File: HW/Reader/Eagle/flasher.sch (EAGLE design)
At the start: 26 parts, among them Q1 12Mhz, Q1A MMBT3904, Q1B MMBT3904, X1 MINI-USB-SCHIELD-32005-201

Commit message: Flasher CH340G SCH & PCB
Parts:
- removed D1: SS14, diode:DIODE-DO-214AC
- removed R8, R9: 470, rcl:R-US_M0805
- removed RX: (no value), led:LEDCHIP-LED0805
- added P3: (no value), pinhead:PINHD-1X6
- added R2: 470, rcl:R-US_M0805
- renumbered Q1A to T1, Q1B to T2, U$1 to U1
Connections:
- removed net N$7: R9.2, TX.A
- removed net VIN: D1.A, P1.1, P2.1, X1G$1.1
- net +5V: now also P1.1, P2.1, P3.1, X1G$1.1; no longer D1.C, R8.1, R9.1
- net GND: now also P3.6, TX.C
- net GPIO0: now also P3.4
- net N$1: now also R2.2; no longer TX.C
- net N$2: no longer RX.C
- net N$4: now also R2.1, TX.A; no longer R8.2, RX.A
- net RESET: now also P3.5
- net RXD: now also P3.2
- net TXD: now also P3.3
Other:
- note added: "ESP8266 Auto Flasher over USB (CH340G)"
- moved on the sheet: R1, R4, TX

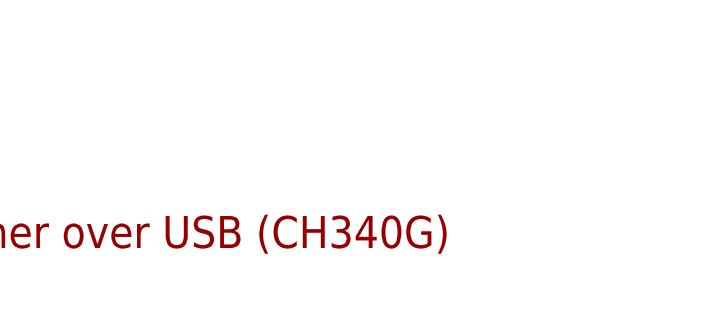
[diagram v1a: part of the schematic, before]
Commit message: Flasher Update
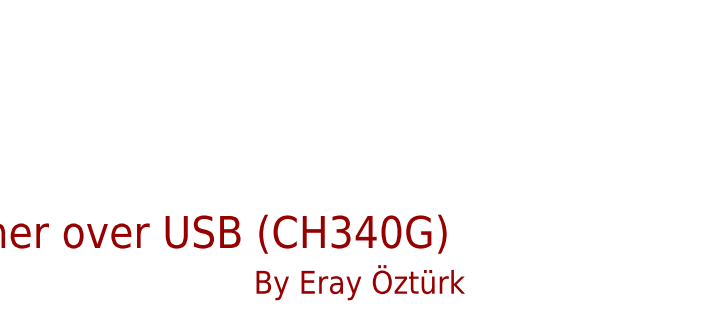
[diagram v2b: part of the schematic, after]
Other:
- note added: "By Eray Öztürk"
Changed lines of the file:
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@@
 <grid distance="0.1" unitdist="inch" unit="inch" style="lines" multiple="1" display="no" altdistance="0.01" altunitdist="inch" altunit="inch"/>
 <layers>
-<layer number="1" name="Top" color="4" fill="1" visible="no" active="no"/>
-<layer number="16" name="Bottom" color="1" fill="1" visible="no" active="no"/>
-<layer number="17" name="Pads" color="2" fill="1" visible="no" active="no"/>
-<layer number="18" name="Vias" color="2" fill="1" visible="no" active="no"/>
-<layer number="19" name="Unrouted" color="6" fill="1" visible="no" active="no"/>
-<layer number="20" name="Dimension" color="24" fill="1" visible="no" active="no"/>
-<layer number="21" name="tPlace" color="7" fill="1" visible="no" active="no"/>
-<layer number="22" name="bPlace" color="7" fill="1" visible="no" active="no"/>
-<layer number="23" name="tOrigins" color="15" fill="1" visible="no" active="no"/>
-<layer number="24" name="bOrigins" color="15" fill="1" visible="no" active="no"/>
-<layer number="25" name="tNames" color="7" fill="1" visible="no" active="no"/>
-<layer number="26" name="bNames" color="7" fill="1" visible="no" active="no"/>
-<layer number="27" name="tValues" color="7" fill="1" visible="no" active="no"/>
-<layer number="28" name="bValues" color="7" fill="1" visible="no" active="no"/>
+<layer number="1" name="Top" color="4" fill="1" visible="yes" active="no"/>
+<layer number="16" name="Bottom" color="1" fill="1" visible="yes" active="no"/>
+<layer number="17" name="Pads" color="2" fill="1" visible="yes" active="no"/>
+<layer number="18" name="Vias" color="2" fill="1" visible="yes" active="no"/>
+<layer number="19" name="Unrouted" color="6" fill="1" visible="yes" active="no"/>
+<layer number="20" name="Dimension" color="24" fill="1" visible="yes" active="no"/>
+<layer number="21" name="tPlace" color="7" fill="1" visible="yes" active="no"/>
+<layer number="22" name="bPlace" color="7" fill="1" visible="yes" active="no"/>
+<layer number="23" name="tOrigins" color="15" fill="1" visible="yes" active="no"/>
+<layer number="24" name="bOrigins" color="15" fill="1" visible="yes" active="no"/>
+<layer number="25" name="tNames" color="7" fill="1" visible="yes" active="no"/>
+<layer number="26" name="bNames" color="7" fill="1" visible="yes" active="no"/>
+<layer number="27" name="tValues" color="7" fill="1" visible="yes" active="no"/>
+<layer number="28" name="bValues" color="7" fill="1" visible="yes" active="no"/>
 <layer number="29" name="tStop" color="7" fill="3" visible="no" active="no"/>
 <layer number="30" name="bStop" color="7" fill="6" visible="no" active="no"/>
@@
 <layer number="35" name="tGlue" color="7" fill="4" visible="no" active="no"/>
 <layer number="36" name="bGlue" color="7" fill="5" visible="no" active="no"/>
-<layer number="37" name="tTest" color="7" fill="1" visible="no" active="no"/>
-<layer number="38" name="bTest" color="7" fill="1" visible="no" active="no"/>
+<layer number="37" name="tTest" color="7" fill="1" visible="yes" active="no"/>
+<layer number="38" name="bTest" color="7" fill="1" visible="yes" active="no"/>
 <layer number="39" name="tKeepout" color="4" fill="11" visible="no" active="no"/>
 <layer number="40" name="bKeepout" color="1" fill="11" visible="no" active="no"/>
@@
 <layer number="44" name="Drills" color="7" fill="1" visible="no" active="no"/>
 <layer number="45" name="Holes" color="7" fill="1" visible="no" active="no"/>
-<layer number="46" name="Milling" color="3" fill="1" visible="no" active="no"/>
-<layer number="47" name="Measures" color="7" fill="1" visible="no" active="no"/>
-<layer number="48" name="Document" color="7" fill="1" visible="no" active="no"/>
-<layer number="49" name="Reference" color="7" fill="1" visible="no" active="no"/>
-<layer number="50" name="dxf" color="7" fill="1" visible="no" active="no"/>
-<layer number="51" name="tDocu" color="7" fill="1" visible="no" active="no"/>
-<layer number="52" name="bDocu" color="7" fill="1" visible="no" active="no"/>
-<layer number="53" name="tGND_GNDA" color="7" fill="9" visible="no" active="no"/>
-<layer number="54" name="bGND_GNDA" color="1" fill="9" visible="no" active="no"/>
-<layer number="56" name="wert" color="7" fill="1" visible="no" active="no"/>
-<layer number="57" name="tCAD" color="7" fill="1" visible="no" active="no"/>
-<layer number="59" name="tCarbon" color="7" fill="1" visible="no" active="no"/>
-<layer number="60" name="bCarbon" color="7" fill="1" visible="no" active="no"/>
+<layer number="46" name="Milling" color="3" fill="1" visible="yes" active="no"/>
+<layer number="47" name="Measures" color="7" fill="1" visible="yes" active="no"/>
+<layer number="48" name="Document" color="7" fill="1" visible="yes" active="no"/>
+<layer number="49" name="Reference" color="7" fill="1" visible="yes" active="no"/>
+<layer number="50" name="dxf" color="7" fill="1" visible="yes" active="no"/>
+<layer number="51" name="tDocu" color="7" fill="1" visible="yes" active="no"/>
+<layer number="52" name="bDocu" color="7" fill="1" visible="yes" active="no"/>
+<layer number="53" name="tGND_GNDA" color="7" fill="9" visible="yes" active="no"/>
+<layer number="54" name="bGND_GNDA" color="1" fill="9" visible="yes" active="no"/>
+<layer number="56" name="wert" color="7" fill="1" visible="yes" active="no"/>
+<layer number="57" name="tCAD" color="7" fill="1" visible="yes" active="no"/>
+<layer number="59" name="tCarbon" color="7" fill="1" visible="yes" active="no"/>
+<layer number="60" name="bCarbon" color="7" fill="1" visible="yes" active="no"/>
 <layer number="88" name="SimResults" color="9" fill="1" visible="yes" active="yes"/>
 <layer number="89" name="SimProbes" color="9" fill="1" visible="yes" active="yes"/>
@@
 <part name="R3" library="rcl" library_urn="urn:adsk.eagle:library:334" deviceset="R-US_" device="M0805" package3d_urn="urn:adsk.eagle:package:23556/2" value="12k"/>
 <part name="R6" library="rcl" library_urn="urn:adsk.eagle:library:334" deviceset="R-US_" device="M0805" package3d_urn="urn:adsk.eagle:package:23556/2" value="12k"/>
-<part name="T1" library="MMBT3904" deviceset="MMBT3904" device=""/>
-<part name="T2" library="MMBT3904" deviceset="MMBT3904" device=""/>
+<part name="T1" library="MMBT3904" deviceset="MMBT3904" device="" override_package3d_urn="urn:adsk.eagle:package:19129588/2" override_package_urn="urn:adsk.eagle:footprint:19129589/1"/>
+<part name="T2" library="MMBT3904" deviceset="MMBT3904" device="" override_package3d_urn="urn:adsk.eagle:package:19129585/2" override_package_urn="urn:adsk.eagle:footprint:19129586/1"/>
 <part name="C11" library="rcl" library_urn="urn:adsk.eagle:library:334" deviceset="C-EU" device="C0805" package3d_urn="urn:adsk.eagle:package:23617/2" value="100nF"/>
 <part name="GND1" library="supply1" library_urn="urn:adsk.eagle:library:371" deviceset="GND" device=""/>
@@
 <part name="X1" library="con-cypressindustries" library_urn="urn:adsk.eagle:library:138" deviceset="MINI-USB-SCHIELD-" device="32005-201" package3d_urn="urn:adsk.eagle:package:6443/1"/>
 <part name="PWR" library="led" library_urn="urn:adsk.eagle:library:259" deviceset="LED" device="CHIP-LED0805" package3d_urn="urn:adsk.eagle:package:15818/2"/>
-<part name="U1" library="ch340g" deviceset="CH340G" device=""/>
+<part name="U1" library="ch340g" deviceset="CH340G" device="" override_package3d_urn="urn:adsk.eagle:package:19129574/2" override_package_urn="urn:adsk.eagle:footprint:19129575/1"/>
 <part name="Q1" library="crystal" library_urn="urn:adsk.eagle:library:204" deviceset="CRYSTAL" device="HC49S" package3d_urn="urn:adsk.eagle:package:12071/1" value="12Mhz"/>
 <part name="C1" library="rcl" library_urn="urn:adsk.eagle:library:334" deviceset="C-EU" device="C0805" package3d_urn="urn:adsk.eagle:package:23617/2" value="22pF"/>
@@
 <plain>
 <text x="58.42" y="-48.26" size="3.556" layer="94">ESP8266 Auto Flasher over USB (CH340G)</text>
+<text x="129.54" y="-53.34" size="2.54" layer="94">By Eray Öztürk</text>
 </plain>
 <instances>
@@
 packages will not be understood (or retained) with this version.
 </note>
+<note version="9.4" severity="warning">
+Since Version 9.4, EAGLE supports the overriding of 3D packages
+in schematics and board files. Those overridden 3d packages
+will not be understood (or retained) with this version.
+</note>
 <note version="8.4" severity="warning">
